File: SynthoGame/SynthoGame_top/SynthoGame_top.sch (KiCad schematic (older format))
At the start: 21 parts, among them U7 AT42QT1244

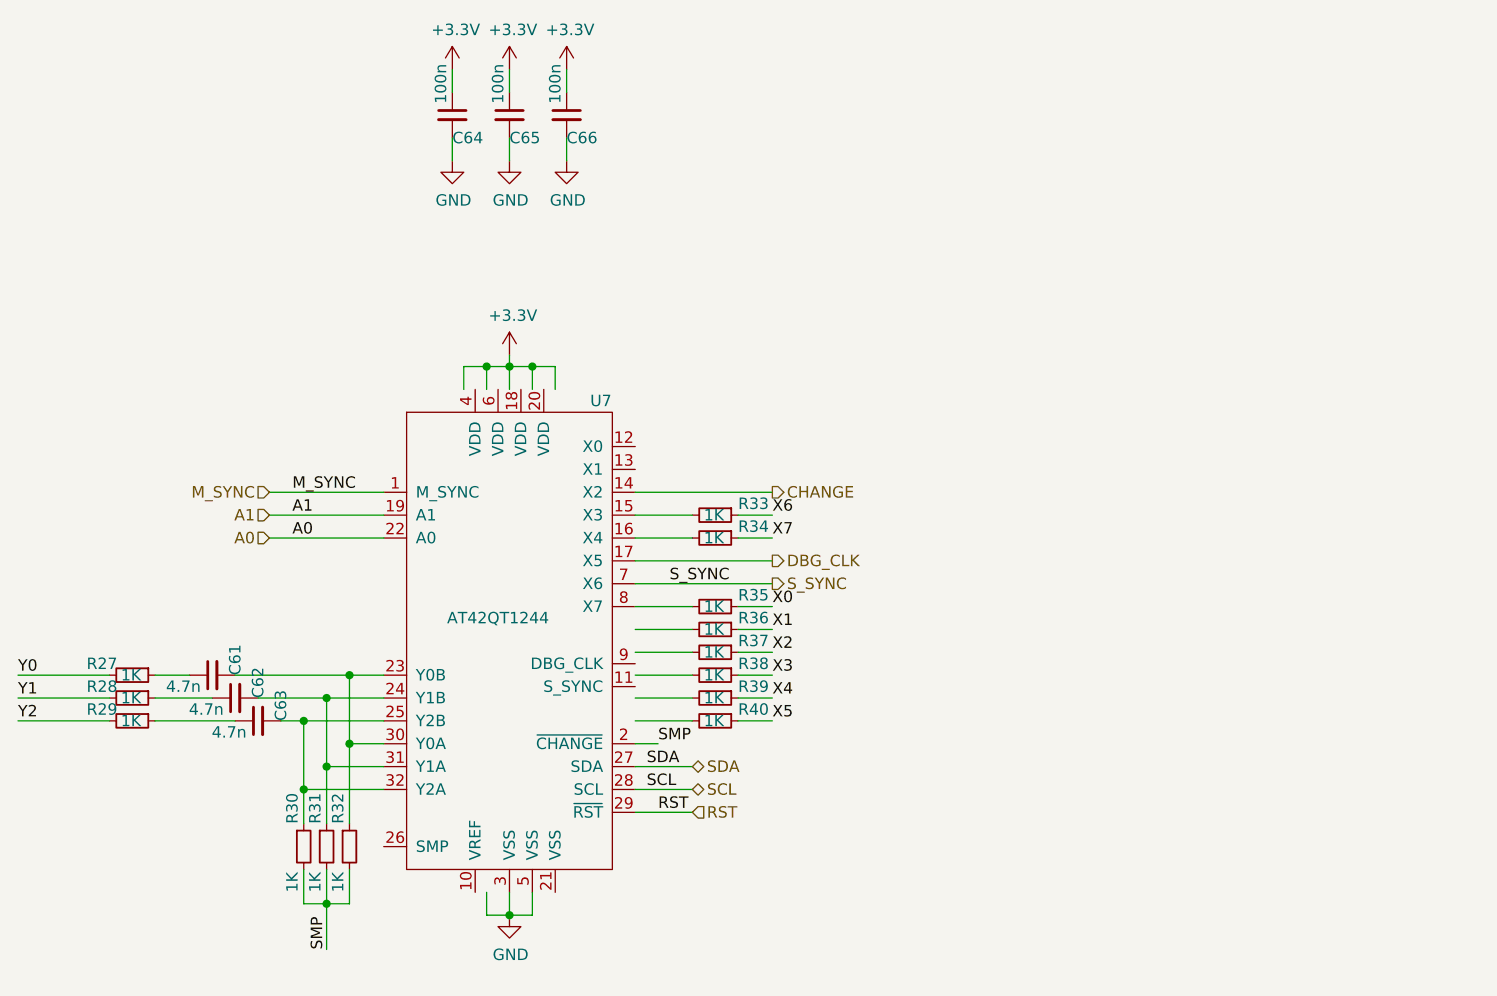
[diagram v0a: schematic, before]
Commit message: Adding connector
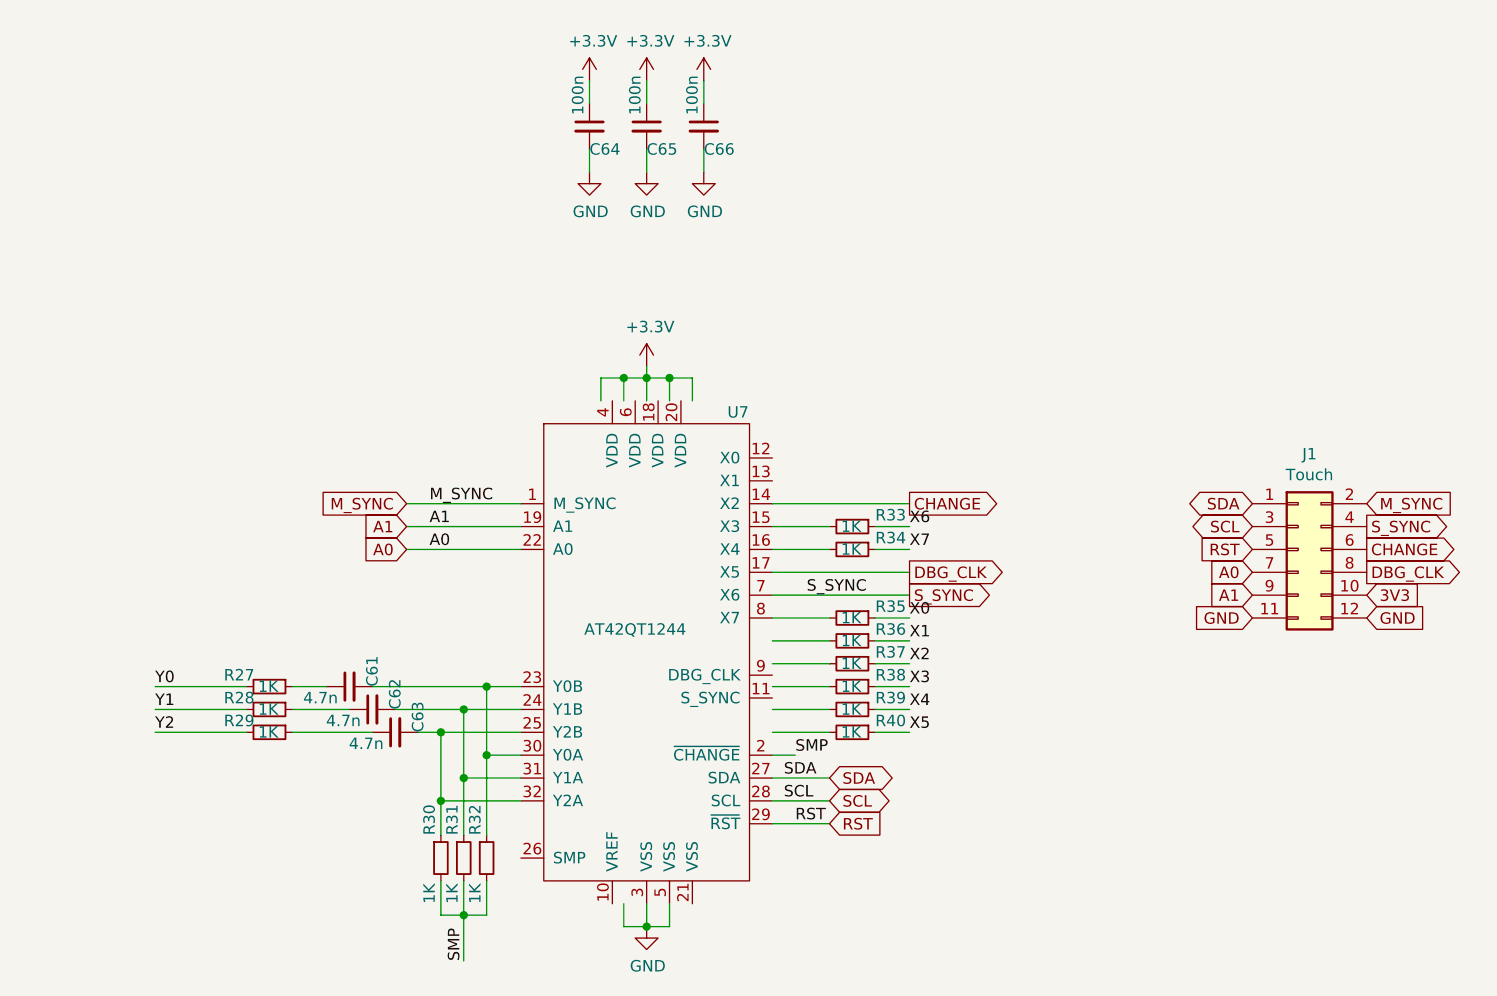
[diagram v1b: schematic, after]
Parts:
- added J1: Touch, Connector_PinHeader_2.54mm:PinHeader_2x06_P2.54mm_Vertical_SMD, symbol Connector_Generic:Conn_02x06_Odd_Even
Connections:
- net labels added: 3V3
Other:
- moved on the sheet: C61, C62, C63, C64, C65, C66, R27, R28, R29, R30, R31, R32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

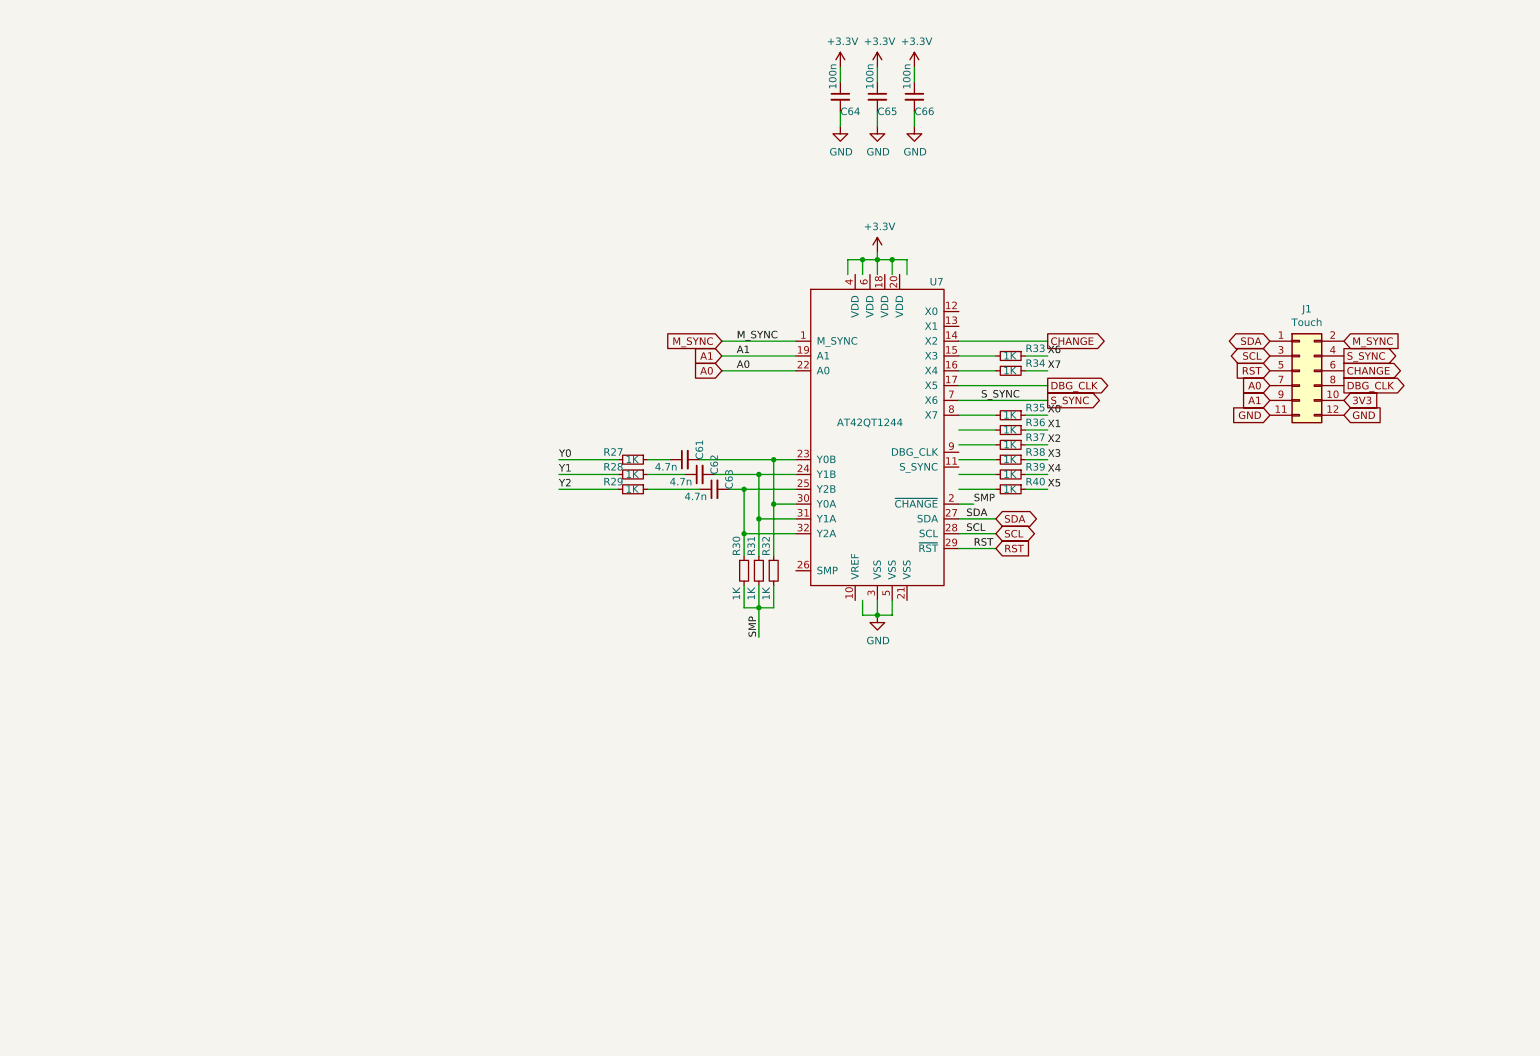
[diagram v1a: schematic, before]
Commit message: fix top board wiring, add touch key footprint, adjust connector position
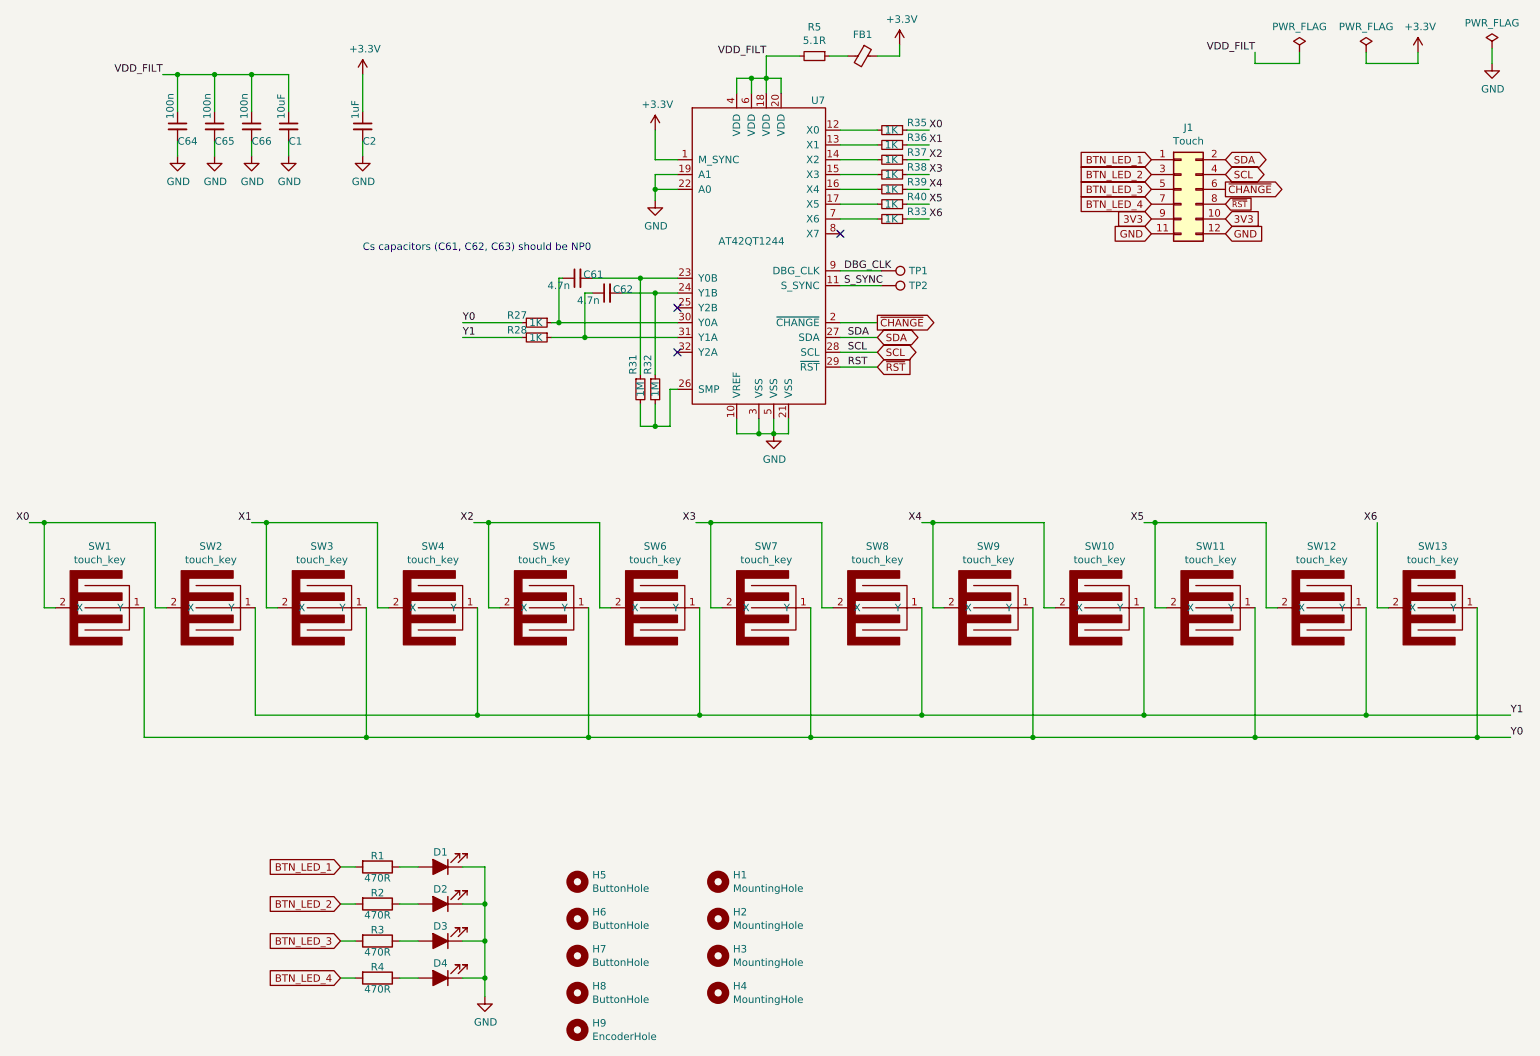
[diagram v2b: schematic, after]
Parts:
- removed C63: 4.7n, Capacitor_SMD:C_0402_1005Metric, symbol Device:C_Small
- removed R29, R30, R34: 1K, Resistor_SMD:R_0402_1005Metric, symbol Device:R_Small
- added C1: 10uF, Capacitor_SMD:C_0603_1608Metric, symbol Device:C_Small
- added C2: 1uF, Capacitor_SMD:C_0402_1005Metric, symbol Device:C_Small
- added D1, D2, D3, D4: LED_ALT, LED_SMD:LED_0603_1608Metric, symbol Device:LED_ALT
- added FB1: Ferrite_Bead_Small, Inductor_SMD:L_0402_1005Metric, symbol Device:Ferrite_Bead_Small
- added H1, H2, H3, H4: MountingHole, MountingHole:MountingHole_2.7mm_M2.5, symbol Mechanical:MountingHole
- added H5, H6, H7, H8: ButtonHole, MountingHole:MountingHole_2.7mm_M2.5, symbol Mechanical:MountingHole
- added H9: EncoderHole, MountingHole:MountingHole_2.7mm_M2.5, symbol Mechanical:MountingHole
- added R1, R2, R3, R4: 470R, Resistor_SMD:R_0402_1005Metric, symbol Device:R
- added R5: 5.1R, Resistor_SMD:R_0402_1005Metric, symbol Device:R_Small
- added SW1, SW10, SW11, SW12, SW13, SW2, SW3, SW4, SW5, SW6, SW7, SW8, SW9: touch_key, touch_pad:touch_pad, symbol touch_key:touch_key
- added TP1, TP2: TestPoint, TestPoint:TestPoint_Pad_D1.0mm, symbol Connector:TestPoint
- R31, R32: value 1K -> 1M
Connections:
- net labels added: BTN_LED_1, BTN_LED_2, BTN_LED_3, BTN_LED_4, VDD_FILT, ~CHANGE, ~RST
- net labels removed: A0, A1, CHANGE, M_SYNC, SMP, X7, Y2
- wire segments 74 -> 168
- no-connect marks 0 -> 3
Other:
- note added: "Cs capacitors (C61, C62, C63) should be NP0"
- moved on the sheet: C61, C62, C64, C65, C66, J1, R27, R28, R31, R32, R33, R35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

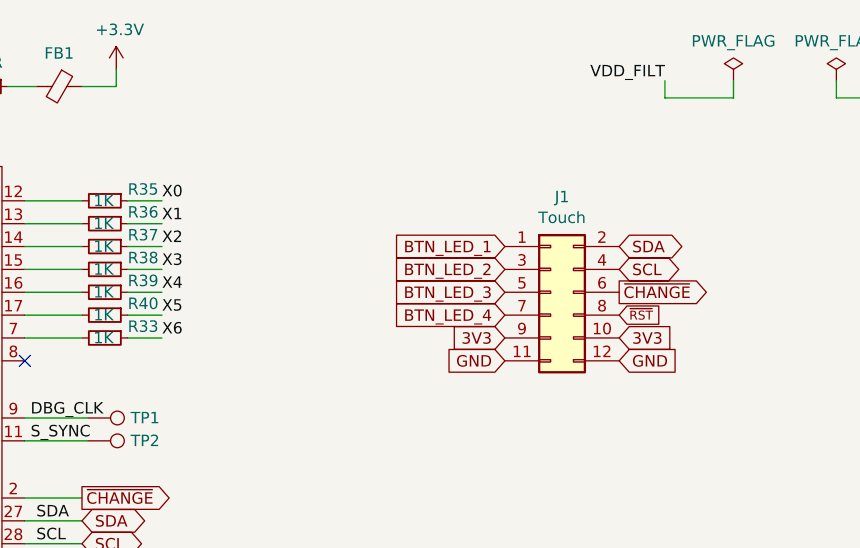
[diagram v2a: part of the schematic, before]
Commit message: Changing X pinout - connecting 3.3V
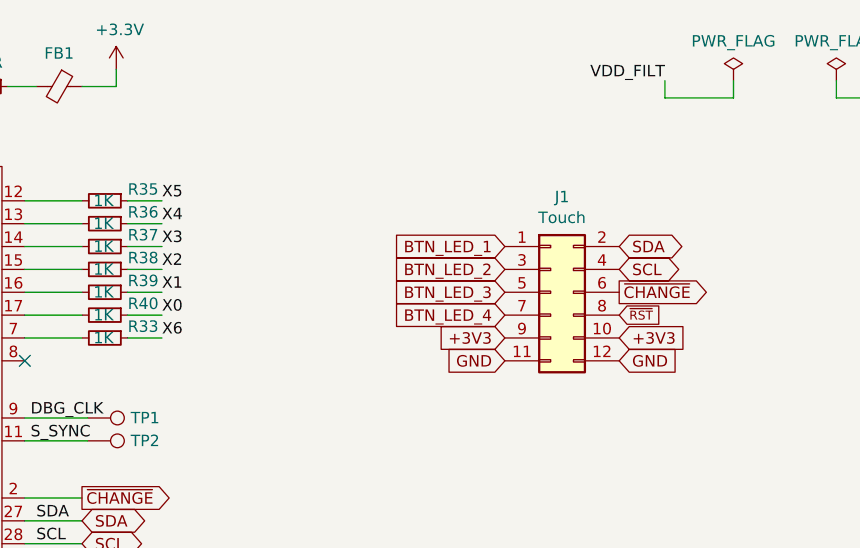
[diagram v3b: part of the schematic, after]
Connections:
- net 3V3 is gone; now on net +3V3: J1.10 (Pin_10), J1.9 (Pin_9)
- net X0: now also R40.1; no longer R35.1
- net X1: now also R39.1; no longer R36.1
- net X2: now also R38.1; no longer R37.1
- net X3: now also R37.1; no longer R38.1
- net X4: now also R36.1; no longer R39.1
- net X5: now also R35.1; no longer R40.1
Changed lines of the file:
@@
 Text Label 6850 2075 0    50   ~ 0
 X6
+Text Label 6850 1975 0    50   ~ 0
+X0
+Text Label 6850 1875 0    50   ~ 0
+X1
+Text Label 6850 1775 0    50   ~ 0
+X2
+Text Label 6850 1675 0    50   ~ 0
+X3
+Text Label 6850 1575 0    50   ~ 0
+X4
 Text Label 6850 1475 0    50   ~ 0
-X0
-Text Label 6850 1575 0    50   ~ 0
-X1
-Text Label 6850 1675 0    50   ~ 0
-X2
-Text Label 6850 1775 0    50   ~ 0
-X3
-Text Label 6850 1875 0    50   ~ 0
-X4
-Text Label 6850 1975 0    50   ~ 0
 X5
 Text Label 3700 2775 0    50   ~ 0
@@
 GND
 Text GLabel 8350 2075 0    50   Input ~ 0
-3V3
++3V3
 Text GLabel 8850 2175 2    50   Input ~ 0
 GND
@@
 BTN_LED_4
 Text GLabel 8850 2075 2    50   Input ~ 0
-3V3
++3V3
 Wire Wire Line
 	10775 5575 10550 5575

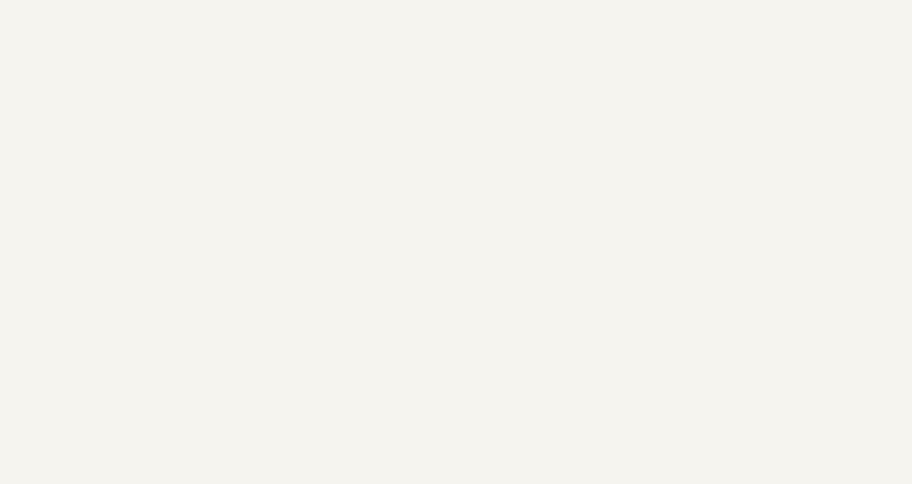
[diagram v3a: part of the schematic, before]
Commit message: add graphic overlays
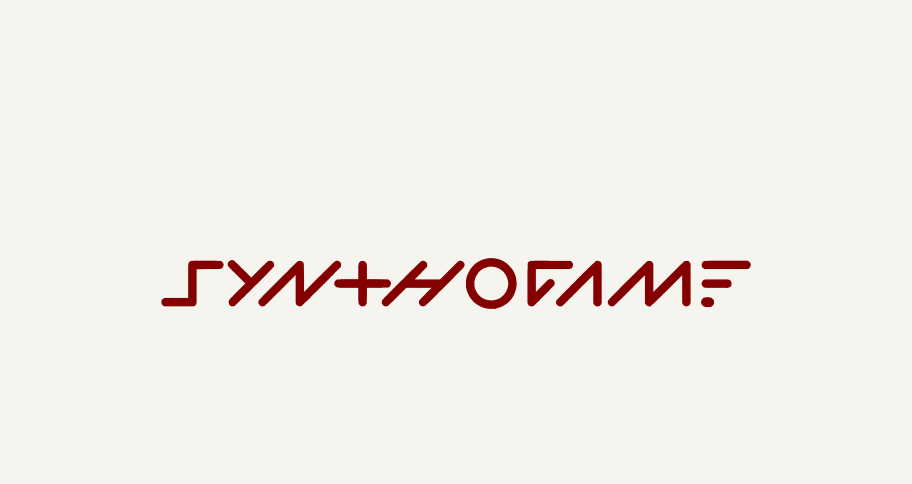
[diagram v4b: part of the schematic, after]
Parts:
- added G1: LOGO, overlays:top_overlay, symbol logo:LOGO
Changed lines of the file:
@@
 	8375 4125 9125 4125
 Connection ~ 8375 4125
+$Comp
+L logo:LOGO G1
+U 1 1 61A4E715
+P 8425 6850
+F 0 "G1" H 8425 6715 60  0001 C CNN
+F 1 "LOGO" H 8425 6985 60  0001 C CNN
+F 2 "overlays:top_overlay" H 8425 6850 50  0001 C CNN
+F 3 "" H 8425 6850 50  0001 C CNN
+	1    8425 6850
+	1    0    0    -1
+$EndComp
 $EndSCHEMATC
